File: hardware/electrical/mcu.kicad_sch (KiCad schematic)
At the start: 43 parts, among them J2 STDC14, SW1 SW_Push, SW2 SW_SPST, U2 STM32F446ZET6, Y1 X322516MLB4SI, Y2 Q13FC1350000400

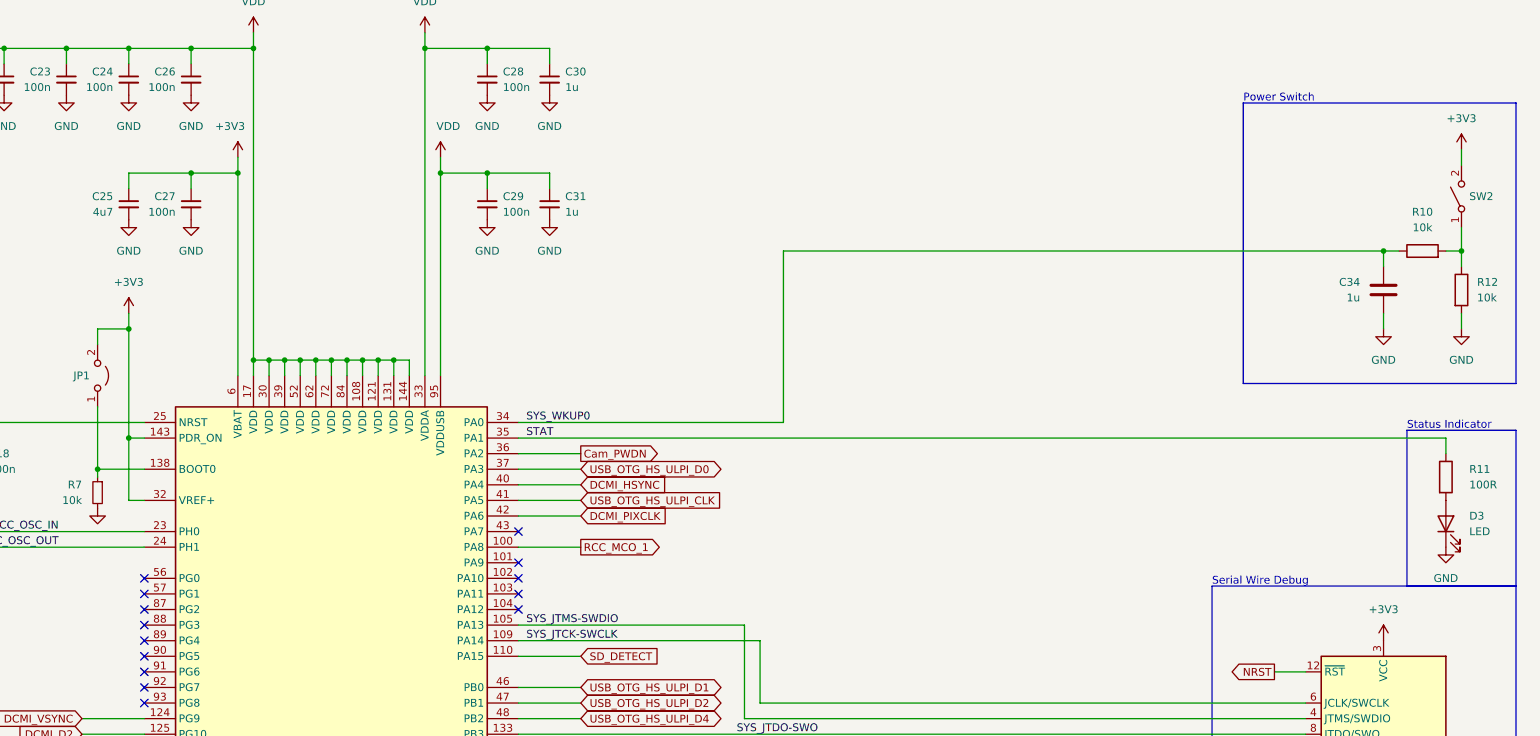
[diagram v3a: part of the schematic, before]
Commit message: Use VDD in place of +3.3V more extensively
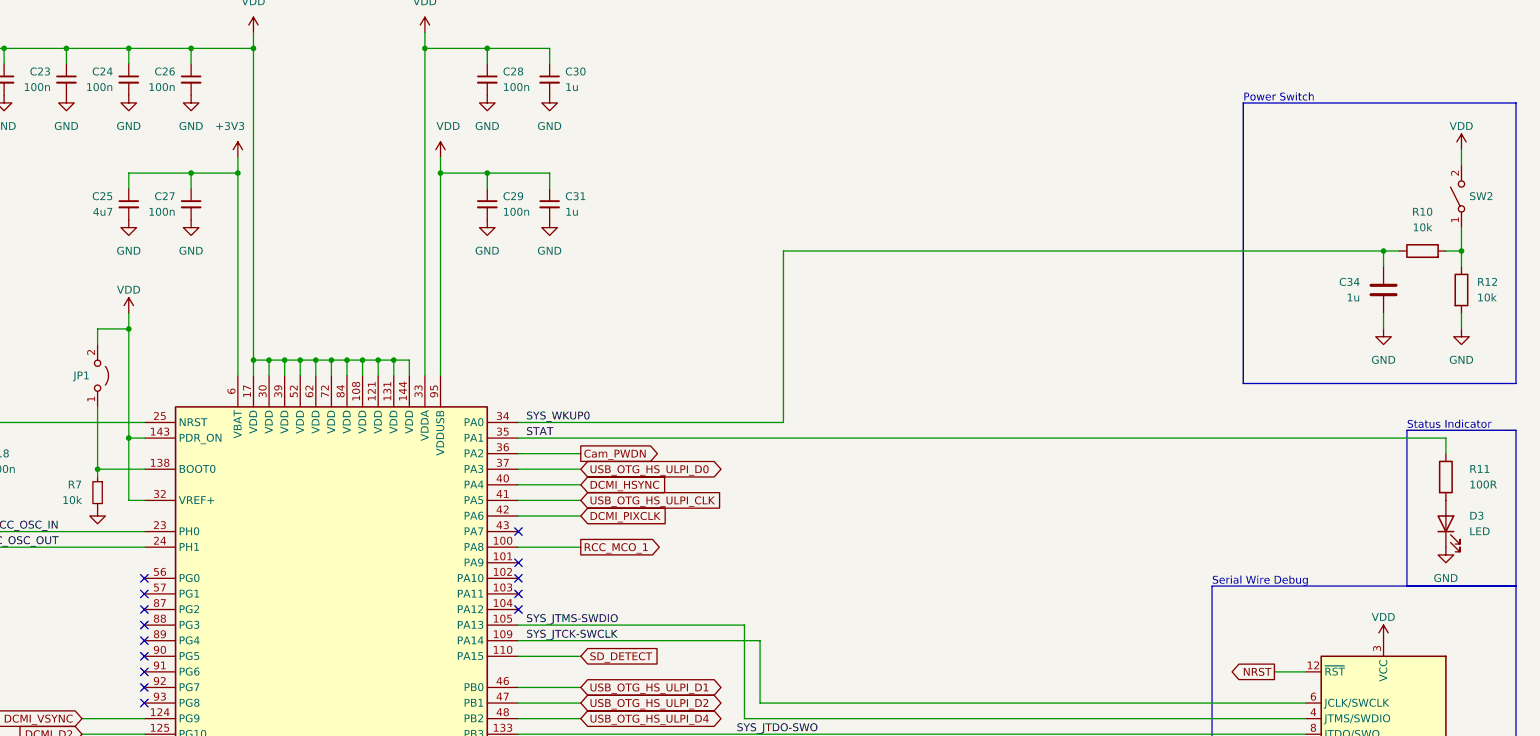
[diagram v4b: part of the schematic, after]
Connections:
- net +3V3: no longer J2.3 (VCC), JP1.2 (B), SW2.2 (B), U2.143 (PDR_ON), U2.32 (VREF+)
- net VDD: now also J2.3 (VCC), JP1.2 (B), SW2.2 (B), U2.143 (PDR_ON), U2.32 (VREF+)
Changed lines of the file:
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@@
+    )
+  )
+  (symbol (lib_id "power:VDD") (at 367.03 121.92 0) (unit 1)
+    (in_bom yes) (on_board yes) (dnp no) (fields_autoplaced)
+    (property "Reference" "#PWR049" (at 367.03 125.73 0)
+      (effects (font (size 1.27 1.27)) hide)
+    )
+    (property "Value" "VDD" (at 367.03 118.11 0)
+      (effects (font (size 1.27 1.27)))
+    )
+    (property "Footprint" "" (at 367.03 121.92 0)
+      (effects (font (size 1.27 1.27)) hide)
+    )
+    (property "Datasheet" "" (at 367.03 121.92 0)
+      (effects (font (size 1.27 1.27)) hide)
+    )
+    (pin "1")
+    (instances
+      (project "3885"
+        (path "/7363a4f0-2da1-4086-abed-ea6709c3a185/239a74a2-fce8-4103-83ba-af4dbf21fb68"
+          (reference "#PWR049") (unit 1)
+        )
+      )
     )
   )
@@
     )
   )
+  (symbol (lib_id "power:VDD") (at 162.56 68.58 0) (unit 1)
+    (in_bom yes) (on_board yes) (dnp no) (fields_autoplaced)
+    (property "Reference" "#PWR033" (at 162.56 72.39 0)
+      (effects (font (size 1.27 1.27)) hide)
+    )
+    (property "Value" "VDD" (at 162.56 64.77 0)
+      (effects (font (size 1.27 1.27)))
+    )
+    (property "Footprint" "" (at 162.56 68.58 0)
+      (effects (font (size 1.27 1.27)) hide)
+    )
+    (property "Datasheet" "" (at 162.56 68.58 0)
+      (effects (font (size 1.27 1.27)) hide)
+    )
+    (pin "1")
+    (instances
+      (project "3885"
+        (path "/7363a4f0-2da1-4086-abed-ea6709c3a185/239a74a2-fce8-4103-83ba-af4dbf21fb68"
+          (reference "#PWR033") (unit 1)
+        )
+      )
+    )
+  )
   (symbol (lib_id "power:GND") (at 379.73 71.12 0) (unit 1)
     (in_bom yes) (on_board yes) (dnp no) (fields_autoplaced)
@@
     )
   )
-  (symbol (lib_id "power:+3V3") (at 162.56 68.58 0) (unit 1)
-    (in_bom yes) (on_board yes) (dnp no) (fields_autoplaced)
-    (property "Reference" "#PWR033" (at 162.56 72.39 0)
-      (effects (font (size 1.27 1.27)) hide)
-    )
-    (property "Value" "+3V3" (at 162.56 63.5 0)
-      (effects (font (size 1.27 1.27)))
-    )
-    (property "Footprint" "" (at 162.56 68.58 0)
-      (effects (font (size 1.27 1.27)) hide)
-    )
-    (property "Datasheet" "" (at 162.56 68.58 0)
-      (effects (font (size 1.27 1.27)) hide)
-    )
-    (pin "1")
-    (instances
-      (project "3885"
-        (path "/7363a4f0-2da1-4086-abed-ea6709c3a185/239a74a2-fce8-4103-83ba-af4dbf21fb68"
-          (reference "#PWR033") (unit 1)
-        )
-      )
-    )
-  )
   (symbol (lib_id "Device:C_Small") (at 231.14 50.8 0) (unit 1)
     (in_bom yes) (on_board yes) (dnp no) (fields_autoplaced)
@@
     )
   )
-  (symbol (lib_id "power:+3V3") (at 379.73 41.91 0) (unit 1)
-    (in_bom yes) (on_board yes) (dnp no) (fields_autoplaced)
-    (property "Reference" "#PWR053" (at 379.73 45.72 0)
-      (effects (font (size 1.27 1.27)) hide)
-    )
-    (property "Value" "+3V3" (at 379.73 36.83 0)
-      (effects (font (size 1.27 1.27)))
-    )
-    (property "Footprint" "" (at 379.73 41.91 0)
-      (effects (font (size 1.27 1.27)) hide)
-    )
-    (property "Datasheet" "" (at 379.73 41.91 0)
-      (effects (font (size 1.27 1.27)) hide)
-    )
-    (pin "1")
-    (instances
-      (project "3885"
-        (path "/7363a4f0-2da1-4086-abed-ea6709c3a185/239a74a2-fce8-4103-83ba-af4dbf21fb68"
-          (reference "#PWR053") (unit 1)
-        )
-      )
-    )
-  )
   (symbol (lib_id "Device:C_Small") (at 81.28 30.48 0) (mirror y) (unit 1)
     (in_bom yes) (on_board yes) (dnp no) (fields_autoplaced)
@@
     )
   )
+  (symbol (lib_id "power:VDD") (at 379.73 41.91 0) (unit 1)
+    (in_bom yes) (on_board yes) (dnp no) (fields_autoplaced)
+    (property "Reference" "#PWR053" (at 379.73 45.72 0)
+      (effects (font (size 1.27 1.27)) hide)
+    )
+    (property "Value" "VDD" (at 379.73 38.1 0)
+      (effects (font (size 1.27 1.27)))
+    )
+    (property "Footprint" "" (at 379.73 41.91 0)
+      (effects (font (size 1.27 1.27)) hide)
+    )
+    (property "Datasheet" "" (at 379.73 41.91 0)
+      (effects (font (size 1.27 1.27)) hide)
+    )
+    (pin "1")
+    (instances
+      (project "3885"
+        (path "/7363a4f0-2da1-4086-abed-ea6709c3a185/239a74a2-fce8-4103-83ba-af4dbf21fb68"
+          (reference "#PWR053") (unit 1)
+        )
+      )
+    )
+  )
   (symbol (lib_id "Device:C_Small") (at 172.72 50.8 0) (mirror y) (unit 1)
     (in_bom yes) (on_board yes) (dnp no) (fields_autoplaced)
@@
         )
       )
-    )
-  )
-  (symbol (lib_id "power:+3V3") (at 367.03 121.92 0) (unit 1)
-    (in_bom yes) (on_board yes) (dnp no) (fields_autoplaced)
-    (property "Reference" "#PWR049" (at 367.03 125.73 0)
-      (effects (font (size 1.27 1.27)) hide)
-    )
-    (property "Value" "+3V3" (at 367.03 116.84 0)
-      (effects (font (size 1.27 1.27)))
-    )
-    (property "Footprint" "" (at 367.03 121.92 0)
-      (effects (font (size 1.27 1.27)) hide)
-    )
-    (property "Datasheet" "" (at 367.03 121.92 0)
-      (effects (font (size 1.27 1.27)) hide)
-    )
-    (pin "1")
-    (instances
-      (project "3885"
-        (path "/7363a4f0-2da1-4086-abed-ea6709c3a185/239a74a2-fce8-4103-83ba-af4dbf21fb68"
-          (reference "#PWR049") (unit 1)
-        )
-      )

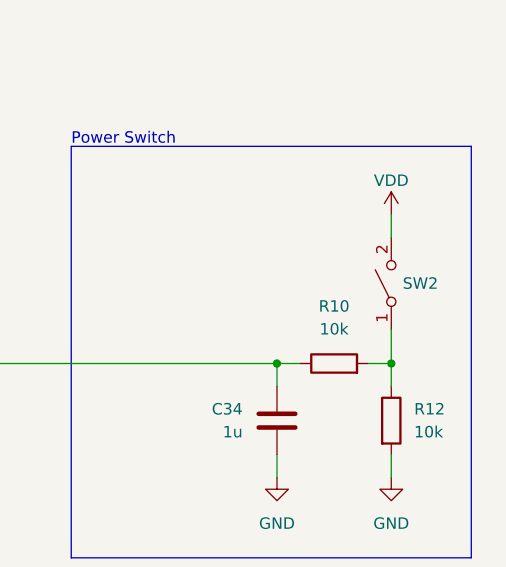
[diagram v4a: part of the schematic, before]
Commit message: Replace SW2 with a momentary switch
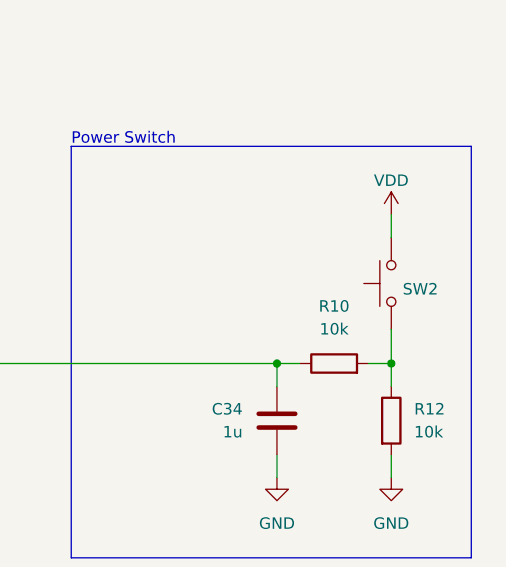
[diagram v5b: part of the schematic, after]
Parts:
- removed SW2: SW_SPST, symbol Switch:SW_SPST
- added SW2: SW_Push, symbol Switch:SW_Push
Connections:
- net VDD: now also SW2.2
- net at R10.2, R12.1: now also SW2.1
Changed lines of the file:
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@@
-    )
-  )
-  (symbol (lib_id "Switch:SW_SPST") (at 379.73 49.53 90) (unit 1)
-    (in_bom yes) (on_board yes) (dnp no) (fields_autoplaced)
-    (property "Reference" "SW2" (at 381 49.5299 90)
-      (effects (font (size 1.27 1.27)) (justify right))
-    )
-    (property "Value" "SW_SPST" (at 381 50.7999 90)
-      (effects (font (size 1.27 1.27)) (justify right) hide)
-    )
-    (property "Footprint" "" (at 379.73 49.53 0)
-      (effects (font (size 1.27 1.27)) hide)
-    )
-    (property "Datasheet" "~" (at 379.73 49.53 0)
-      (effects (font (size 1.27 1.27)) hide)
-    )
-    (pin "1")
-    (pin "2")
-    (instances
-      (project "3885"
-        (path "/7363a4f0-2da1-4086-abed-ea6709c3a185/239a74a2-fce8-4103-83ba-af4dbf21fb68"
-          (reference "SW2") (unit 1)
-        )
-      )
     )
   )
@@
         )
       )
+    )
+  )
+  (symbol (lib_id "Switch:SW_Push") (at 379.73 49.53 90) (unit 1)
+    (in_bom yes) (on_board yes) (dnp no) (fields_autoplaced)
+    (property "Reference" "SW2" (at 381 50.165 90)
+      (effects (font (size 1.27 1.27)) (justify right))
+    )
+    (property "Value" "SW_Push" (at 381 51.435 90)
+      (effects (font (size 1.27 1.27)) (justify right) hide)
+    )
+    (property "Footprint" "" (at 374.65 49.53 0)
+      (effects (font (size 1.27 1.27)) hide)
+    )
+    (property "Datasheet" "~" (at 374.65 49.53 0)
+      (effects (font (size 1.27 1.27)) hide)
+    )
+    (pin "1")
+    (pin "2")
+    (instances
+      (project "3885"
+        (path "/7363a4f0-2da1-4086-abed-ea6709c3a185/239a74a2-fce8-4103-83ba-af4dbf21fb68"
+          (reference "SW2") (unit 1)
+        )
+      )
